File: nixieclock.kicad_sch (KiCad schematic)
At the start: 57 parts, among them Q1 MMBTA42, Q2 FDS2672CT, Q3 SS8050, U1 UCC3803, U2 K155NA1, U3 PicoW, U4 K155NA1, U5 K155NA1, U6 K155NA1, U7 K155NA1, U8 K155NA1

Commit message: small modifications to pcb
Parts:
- added C15, C16, C17, C18, C20: 0.1uF 16v, Capacitor_SMD:C_0603_1608Metric_Pad1.08x0.95mm_HandSolder, symbol Device:C
- added D3: Green LED, LED_SMD:LED_0805_2012Metric_Pad1.15x1.40mm_HandSolder, symbol Device:LED_Filled
- added D4, D5: LED_Filled, LED_SMD:LED_0805_2012Metric_Pad1.15x1.40mm_HandSolder, symbol Device:LED_Filled
- added Q4: SS8050, Package_TO_SOT_SMD:SOT-23, symbol Transistor_BJT:SS8050
- added R19, R21: 1k, Resistor_SMD:R_0603_1608Metric_Pad0.98x0.95mm_HandSolder, symbol Device:R
- added R20, R22: 140, Resistor_SMD:R_0603_1608Metric_Pad0.98x0.95mm_HandSolder, symbol Device:R_Small
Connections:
- net +3V3: now also D3.2 (A), D4.2 (A), D5.2 (A)
- net +5V: now also C15.1, C16.1, C17.1, C18.1, C20.1
- net GND: now also C15.2, C16.2, C17.2, C18.2, C20.2, Q4.2 (E), R19.1
- net GPIO28: now also R21.2
- new net: D3.1 (K), R19.2
- new net: D5.1 (K), R20.1
- new net: Q4.3 (C), R20.2, R22.2
- new net: Q4.1 (B), R21.1
- new net: D4.1 (K), R22.1
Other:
- moved on the sheet: U3

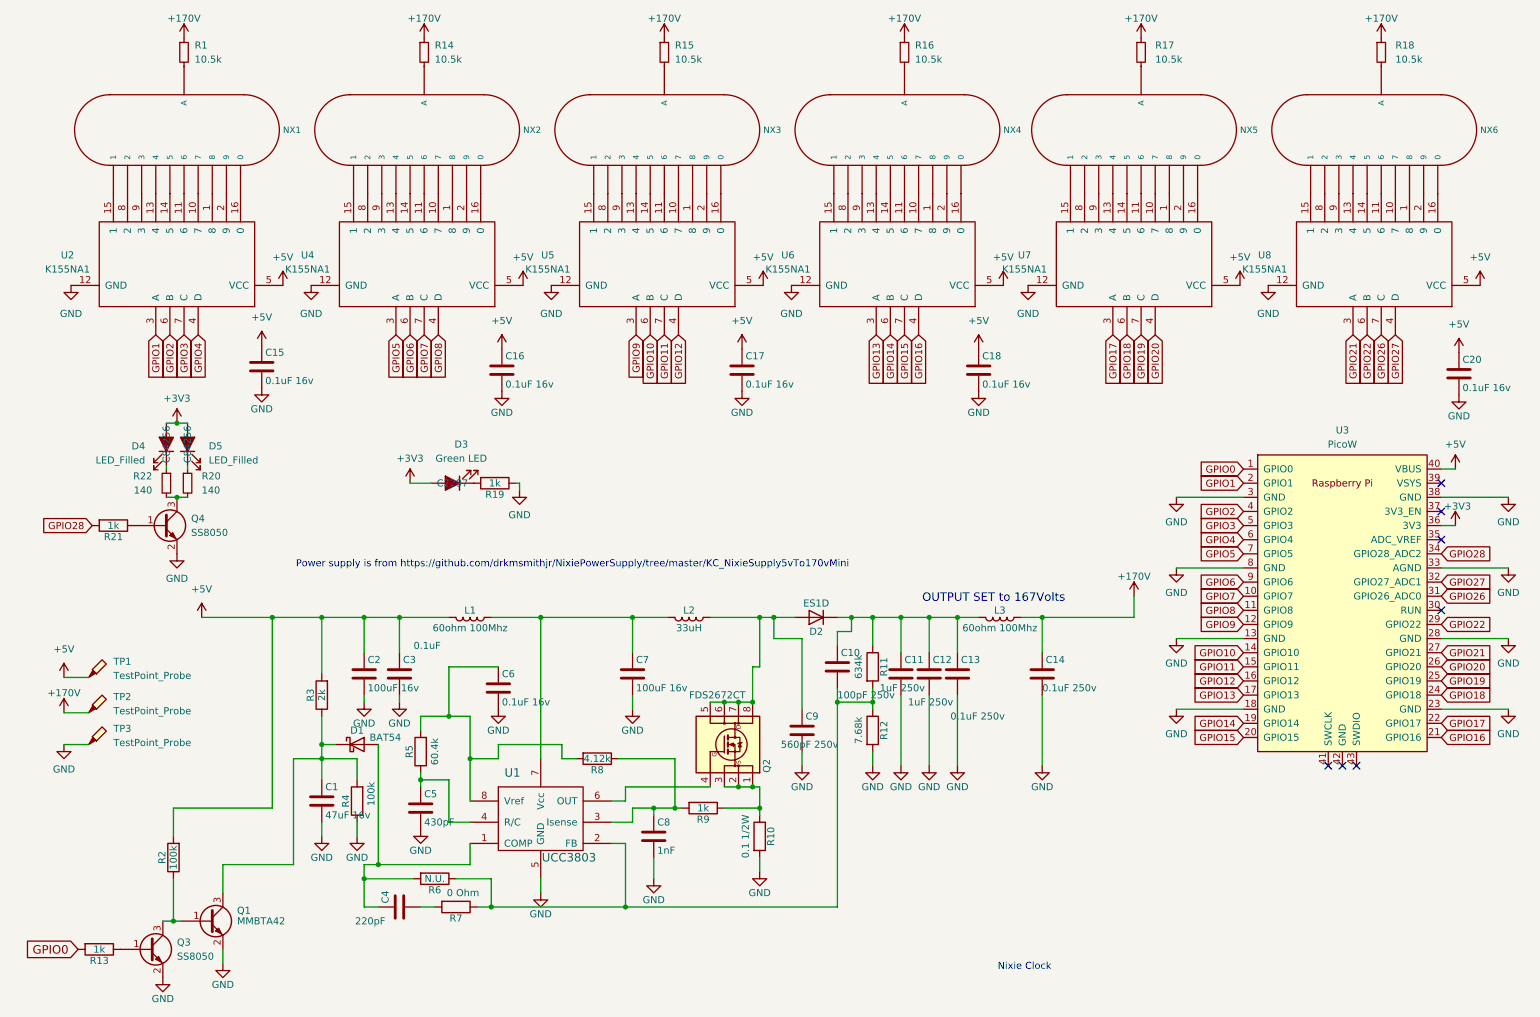
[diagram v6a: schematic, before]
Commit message: Had the footprints for nixies completely wrong, redid them
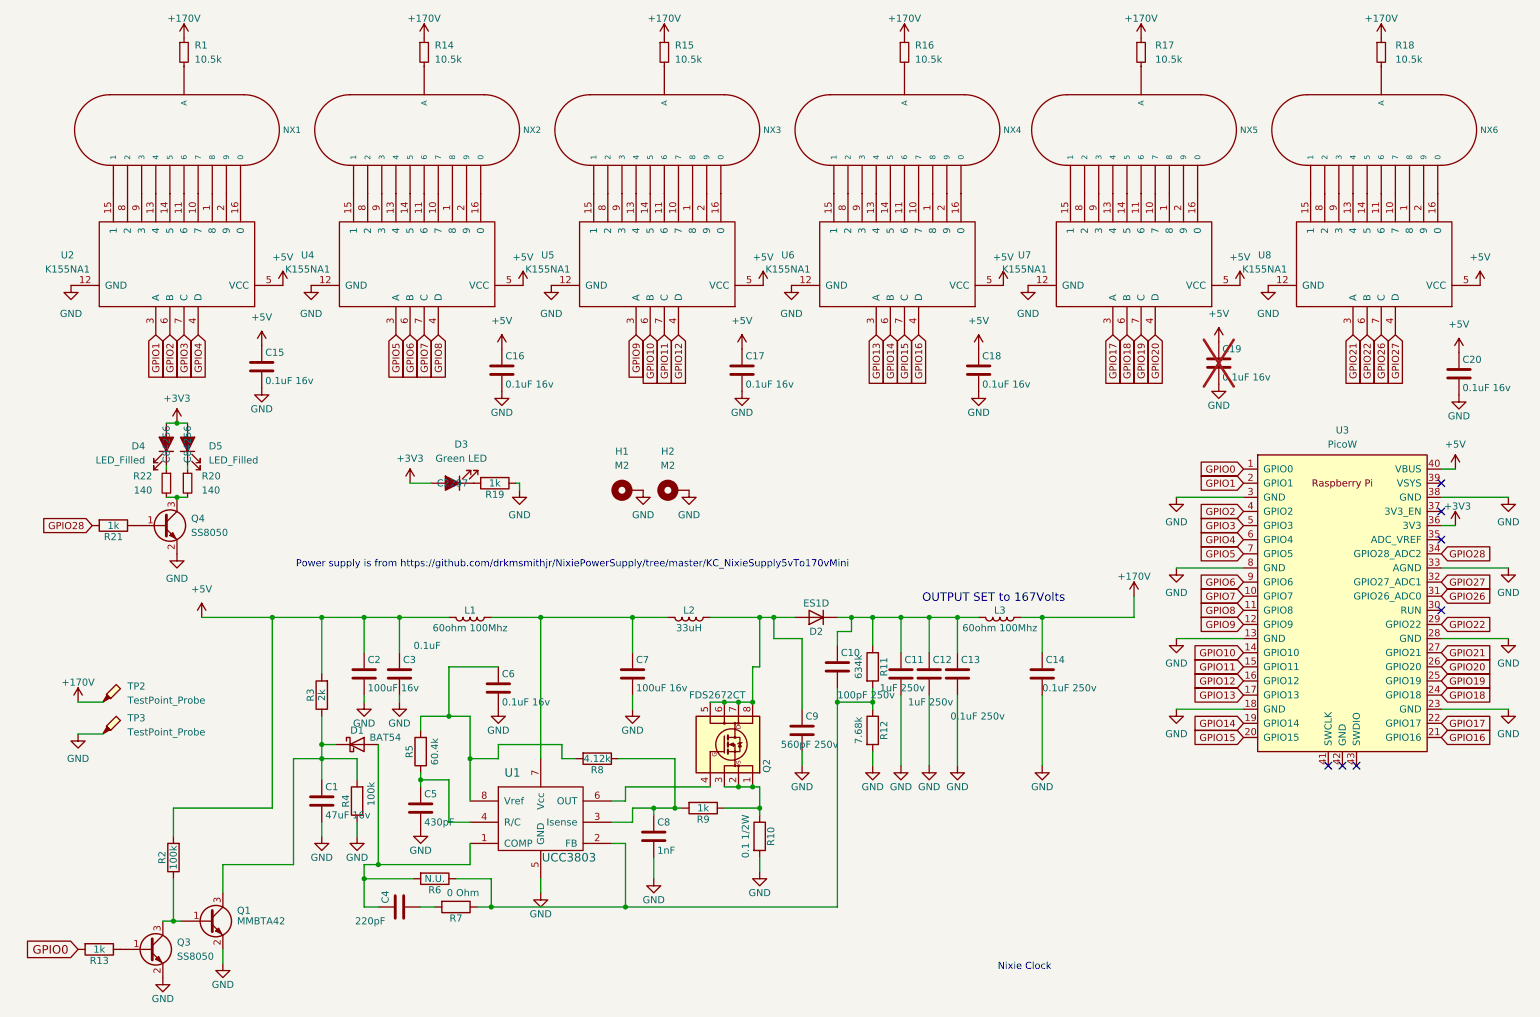
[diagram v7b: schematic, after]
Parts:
- removed TP1: TestPoint_Probe, TestPoint:TestPoint_Pad_2.0x2.0mm, symbol Connector:TestPoint_Probe
- added C19: 0.1uF 16v, Capacitor_SMD:C_0603_1608Metric_Pad1.08x0.95mm_HandSolder, symbol Device:C
- added H1, H2: M2, MountingHole:MountingHole_2.2mm_M2_DIN965_Pad_TopBottom, symbol Mechanical:MountingHole_Pad
- NX1, NX2, NX3, NX4, NX5, NX6: footprint nixies-us:nixies-us-IN-12 -> nixies-us:nixies-us-IN-12-DSUB
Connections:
- net +5V: now also C19.1
- net GND: now also C19.2, H1.1, H2.1
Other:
- moved on the sheet: TP2, TP3

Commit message: add tvs diodes for protection
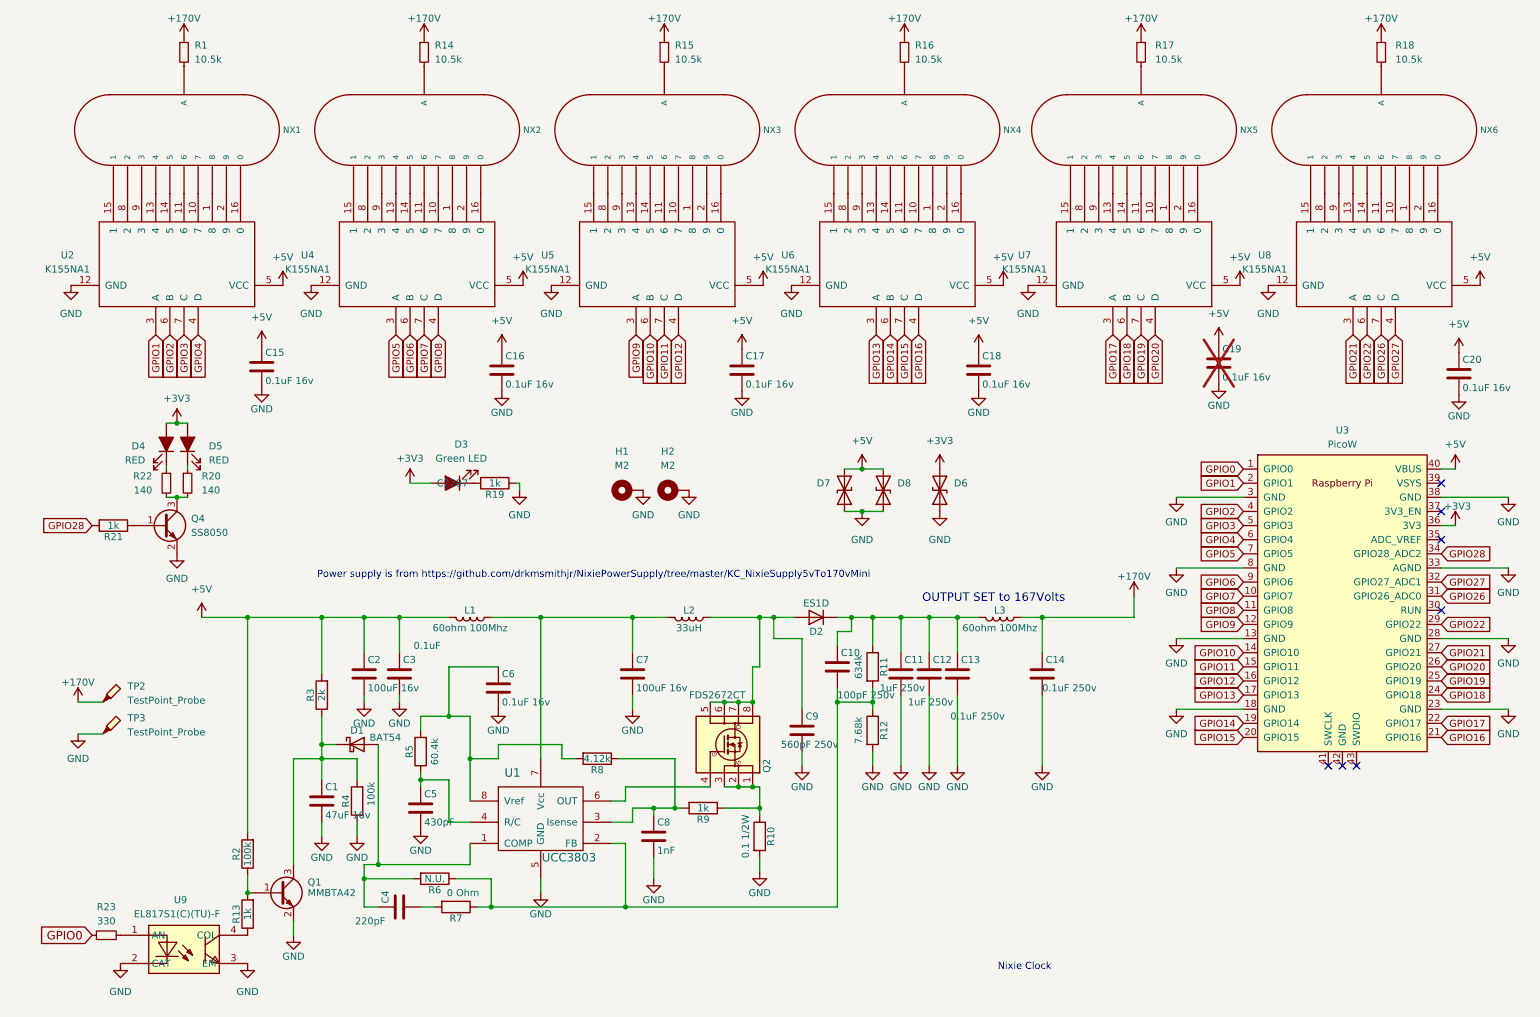
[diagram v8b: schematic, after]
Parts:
- removed Q3: SS8050, Package_TO_SOT_SMD:SOT-23, symbol Transistor_BJT:SS8050
- added D6, D7, D8: PESD5V5C1BLYL, Diode_SMD:D_SOD-882, symbol Device:D_TVS
- added R23: 330, Resistor_SMD:R_0603_1608Metric_Pad0.98x0.95mm_HandSolder, symbol Device:R_Small
- added U9: EL817S1(C)(TU)-F, easyeda2kicad:OPTO-SMD-4_L4.6-W6.5-P2.54-LS10.3-TL, symbol easyeda2kicad:EL817S1(C)(TU)-F
- D4, D5: value LED_Filled -> RED
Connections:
- net +3V3: now also D6.2 (A2)
- net +5V: now also D7.2 (A2), D8.2 (A2)
- net GND: now also D6.1 (A1), D7.1 (A1), D8.1 (A1), U9.2 (CAT), U9.3 (EM)
- net GPIO0: now also R23.1; no longer R13.2
- net at R13.1: now also U9.4 (COL)
- net at Q1.1 (B), R2.1: now also R13.2
- new net: R23.2, U9.1 (AN)
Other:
- moved on the sheet: Q1, R2
